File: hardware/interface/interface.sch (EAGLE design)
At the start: 3 parts

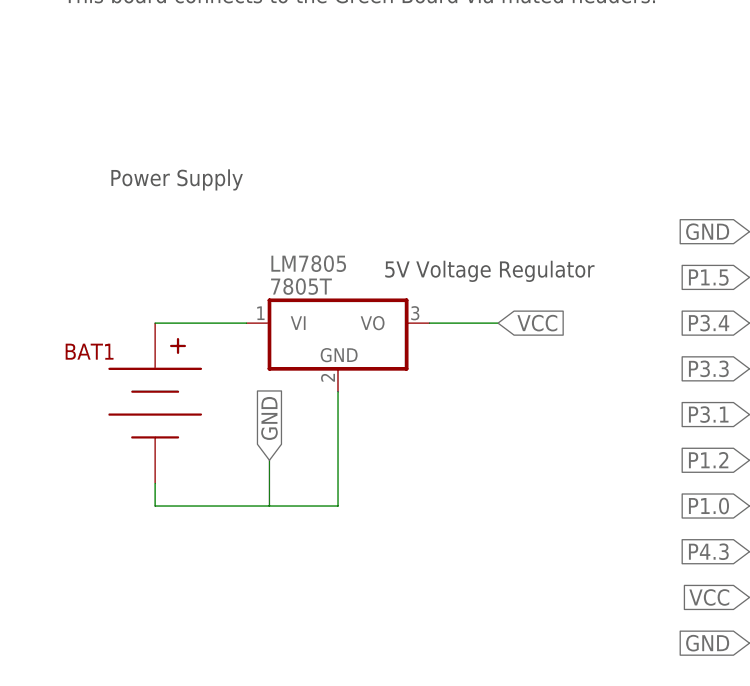
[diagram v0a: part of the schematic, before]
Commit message: add capacitors
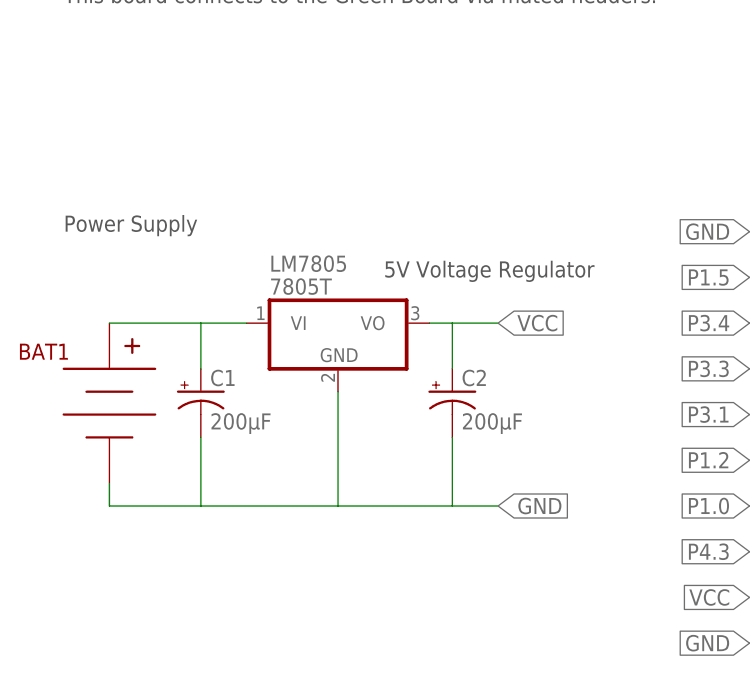
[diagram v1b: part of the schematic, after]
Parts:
- added C1, C2: 200µF, SparkFun-Capacitors:CAP_POLPTH1
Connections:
- net GND: now also C1.-, C2.-
- net N$1: now also C1.+
- net VCC: now also C2.+
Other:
- moved on the sheet: BAT1
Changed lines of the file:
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@@
 <part name="BAT1" library="SparkFun-Connectors" deviceset="BC9VPC" device=""/>
 <part name="LM7805" library="linear" deviceset="78*" device="T" technology="05"/>
+<part name="C1" library="SparkFun-Capacitors" deviceset="CAP_POL" device="PTH1" value="200µF"/>
+<part name="C2" library="SparkFun-Capacitors" deviceset="CAP_POL" device="PTH1" value="200µF"/>
 </parts>
 <sheets>
@@
 <text x="96.52" y="121.92" size="1.778" layer="97">LCD 128x64</text>
 <text x="25.4" y="109.22" size="1.778" layer="97">5V Voltage Regulator</text>
-<text x="-5.08" y="119.38" size="1.778" layer="97">Power Supply</text>
+<text x="-10.16" y="114.3" size="1.778" layer="97">Power Supply</text>
 <frame x1="-20.32" y1="35.56" x2="124.46" y2="154.94" columns="8" rows="5" layer="91"/>
 <text x="-10.16" y="144.78" size="1.778" layer="97">Connects LCD to Green Board and supplies power to the Green Board</text>
@@
 <instances>
 <instance part="U$1" gate="G$1" x="101.6" y="93.98"/>
-<instance part="BAT1" gate="G$1" x="0" y="96.52"/>
+<instance part="BAT1" gate="G$1" x="-5.08" y="96.52"/>
 <instance part="LM7805" gate="A1" x="20.32" y="104.14"/>
+<instance part="C1" gate="G$1" x="5.08" y="96.52"/>
+<instance part="C2" gate="G$1" x="33.02" y="96.52"/>
 </instances>
 <busses>
@@
 <wire x1="20.32" y1="96.52" x2="20.32" y2="83.82" width="0.1524" layer="91"/>
 <pinref part="BAT1" gate="G$1" pin="V-"/>
-<wire x1="20.32" y1="83.82" x2="12.7" y2="83.82" width="0.1524" layer="91"/>
-<wire x1="12.7" y1="83.82" x2="0" y2="83.82" width="0.1524" layer="91"/>
-<wire x1="0" y1="83.82" x2="0" y2="86.36" width="0.1524" layer="91"/>
-<wire x1="12.7" y1="83.82" x2="12.7" y2="88.9" width="0.1524" layer="91"/>
-<label x="12.7" y="88.9" size="1.778" layer="95" rot="R90" xref="yes"/>
+<wire x1="20.32" y1="83.82" x2="5.08" y2="83.82" width="0.1524" layer="91"/>
+<wire x1="5.08" y1="83.82" x2="-5.08" y2="83.82" width="0.1524" layer="91"/>
+<wire x1="-5.08" y1="83.82" x2="-5.08" y2="86.36" width="0.1524" layer="91"/>
+<wire x1="20.32" y1="83.82" x2="33.02" y2="83.82" width="0.1524" layer="91"/>
+<label x="38.1" y="83.82" size="1.778" layer="95" xref="yes"/>
+<pinref part="C1" gate="G$1" pin="-"/>
+<wire x1="33.02" y1="83.82" x2="38.1" y2="83.82" width="0.1524" layer="91"/>
+<wire x1="5.08" y1="91.44" x2="5.08" y2="83.82" width="0.1524" layer="91"/>
+<pinref part="C2" gate="G$1" pin="-"/>
+<wire x1="33.02" y1="91.44" x2="33.02" y2="83.82" width="0.1524" layer="91"/>
 </segment>
 </net>
@@
 <segment>
 <pinref part="LM7805" gate="A1" pin="VO"/>
-<wire x1="30.48" y1="104.14" x2="38.1" y2="104.14" width="0.1524" layer="91"/>
+<wire x1="30.48" y1="104.14" x2="33.02" y2="104.14" width="0.1524" layer="91"/>
 <label x="38.1" y="104.14" size="1.778" layer="95" xref="yes"/>
+<pinref part="C2" gate="G$1" pin="+"/>
+<wire x1="33.02" y1="104.14" x2="38.1" y2="104.14" width="0.1524" layer="91"/>
+<wire x1="33.02" y1="99.06" x2="33.02" y2="104.14" width="0.1524" layer="91"/>
 </segment>
 </net>
@@
 <pinref part="BAT1" gate="G$1" pin="V+"/>
 <pinref part="LM7805" gate="A1" pin="VI"/>
-<wire x1="0" y1="104.14" x2="10.16" y2="104.14" width="0.1524" layer="91"/>
+<wire x1="-5.08" y1="104.14" x2="5.08" y2="104.14" width="0.1524" layer="91"/>
+<pinref part="C1" gate="G$1" pin="+"/>
+<wire x1="5.08" y1="104.14" x2="10.16" y2="104.14" width="0.1524" layer="91"/>
+<wire x1="5.08" y1="99.06" x2="5.08" y2="104.14" width="0.1524" layer="91"/>
 </segment>
 </net>

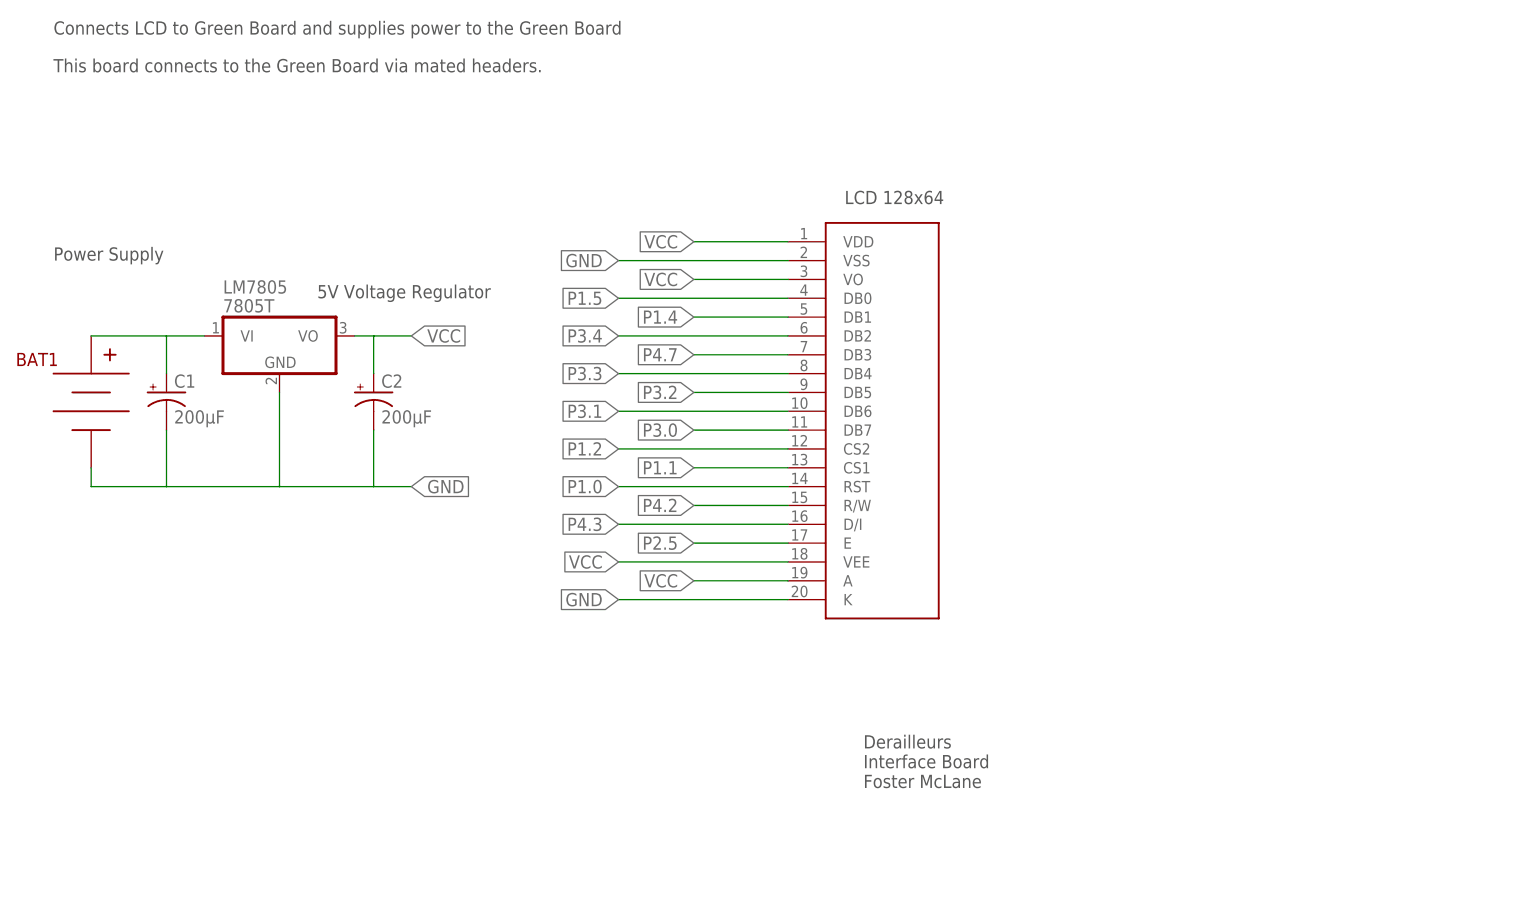
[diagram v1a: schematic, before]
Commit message: update interface schematic
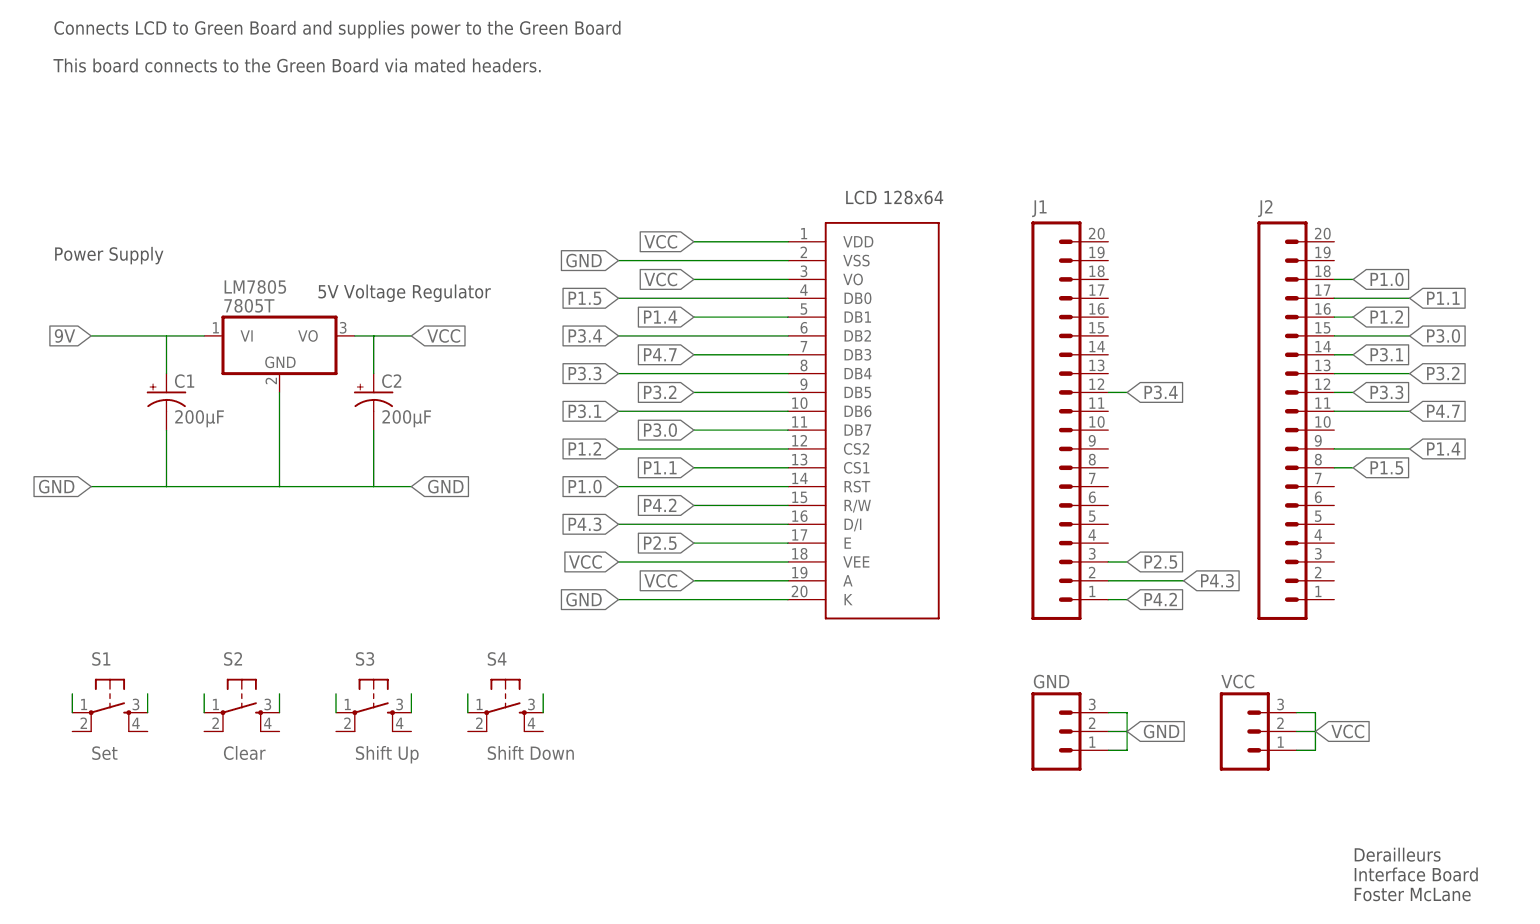
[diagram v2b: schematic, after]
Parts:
- removed BAT1: (no value), SparkFun-Connectors:BC9VPC
- added GND, VCC: (no value), SparkFun-Connectors:M03PTH
- added J1, J2: (no value), SparkFun-Connectors:M20
- added S1: Set, SparkFun-Retired:TAC_SWITCHPTH
- added S2: Clear, SparkFun-Retired:TAC_SWITCHPTH
- added S3: Shift Up, SparkFun-Retired:TAC_SWITCHPTH
- added S4: Shift Down, SparkFun-Retired:TAC_SWITCHPTH
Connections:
- removed net N$1: BAT1.V+, C1.+, LM7805.VI
- new net 9V: C1.+, LM7805.VI
- new net N$2: S1.1
- new net N$3: S1.3
- new net N$4: S2.1
- new net N$5: S2.3
- new net N$6: S3.1
- new net N$7: S3.3
- new net N$8: S4.1
- new net N$9: S4.3
- net GND: now also GND.1, GND.2, GND.3; no longer BAT1.V-
- net P1.0: now also J2.18
- net P1.1: now also J2.17
- net P1.2: now also J2.16
- net P1.4: now also J2.9
- net P1.5: now also J2.8
- net P2.5: now also J1.3
- net P3.0: now also J2.15
- net P3.1: now also J2.14
- net P3.2: now also J2.13
- net P3.3: now also J2.12
- net P3.4: now also J1.12
- net P4.2: now also J1.1
- net P4.3: now also J1.2
- net P4.7: now also J2.11
- net VCC: now also VCC.1, VCC.2, VCC.3

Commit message: finish boards
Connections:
- removed net N$2: S1.1
- removed net N$3: S1.3
- removed net N$4: S2.1
- removed net N$5: S2.3
- removed net N$6: S3.1
- removed net N$7: S3.3
- removed net N$8: S4.1
- removed net N$9: S4.3
- new net P2.0: J1.7, S1.3
- new net P2.6: J1.4, S2.3
- new net P3.5: J1.11, S3.3
- new net P3.6: J1.12, S4.3
- net GND: now also S1.1, S2.1, S3.1, S4.1
- net P3.4: now also J1.10; no longer J1.12
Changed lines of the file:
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@@
 </segment>
 <segment>
-<pinref part="J1" gate="G$1" pin="12"/>
-<wire x1="132.08" y1="96.52" x2="134.62" y2="96.52" width="0.1524" layer="91"/>
-<label x="134.62" y="96.52" size="1.778" layer="95" xref="yes"/>
+<pinref part="J1" gate="G$1" pin="10"/>
+<wire x1="132.08" y1="91.44" x2="134.62" y2="91.44" width="0.1524" layer="91"/>
+<label x="134.62" y="91.44" size="1.778" layer="95" xref="yes"/>
 </segment>
 </net>
@@
 <label x="134.62" y="50.8" size="1.778" layer="95" xref="yes"/>
 </segment>
+<segment>
+<pinref part="S1" gate="S" pin="1"/>
+<wire x1="-7.62" y1="53.34" x2="-7.62" y2="55.88" width="0.1524" layer="91"/>
+<label x="-7.62" y="55.88" size="1.778" layer="95" rot="R90" xref="yes"/>
+</segment>
+<segment>
+<pinref part="S2" gate="S" pin="1"/>
+<wire x1="10.16" y1="53.34" x2="10.16" y2="55.88" width="0.1524" layer="91"/>
+<label x="10.16" y="55.88" size="1.778" layer="95" rot="R90" xref="yes"/>
+</segment>
+<segment>
+<pinref part="S3" gate="S" pin="1"/>
+<wire x1="27.94" y1="53.34" x2="27.94" y2="55.88" width="0.1524" layer="91"/>
+<label x="27.94" y="55.88" size="1.778" layer="95" rot="R90" xref="yes"/>
+</segment>
+<segment>
+<pinref part="S4" gate="S" pin="1"/>
+<wire x1="45.72" y1="53.34" x2="45.72" y2="55.88" width="0.1524" layer="91"/>
+<label x="45.72" y="55.88" size="1.778" layer="95" rot="R90" xref="yes"/>
+</segment>
 </net>
 <net name="VCC" class="0">
@@
 </segment>
 </net>
-<net name="N$2" class="0">
-<segment>
-<pinref part="S1" gate="S" pin="1"/>
-<wire x1="-7.62" y1="53.34" x2="-7.62" y2="55.88" width="0.1524" layer="91"/>
-</segment>
-</net>
-<net name="N$3" class="0">
+<net name="P2.0" class="0">
 <segment>
 <pinref part="S1" gate="S" pin="3"/>
 <wire x1="2.54" y1="53.34" x2="2.54" y2="55.88" width="0.1524" layer="91"/>
+<label x="2.54" y="55.88" size="1.778" layer="95" rot="R90" xref="yes"/>
+</segment>
+<segment>
+<pinref part="J1" gate="G$1" pin="7"/>
+<wire x1="132.08" y1="83.82" x2="134.62" y2="83.82" width="0.1524" layer="91"/>
+<label x="134.62" y="83.82" size="1.778" layer="95" xref="yes"/>
 </segment>
 </net>
-<net name="N$4" class="0">
-<segment>
-<pinref part="S2" gate="S" pin="1"/>
-<wire x1="10.16" y1="53.34" x2="10.16" y2="55.88" width="0.1524" layer="91"/>
-</segment>
-</net>
-<net name="N$5" class="0">
+<net name="P2.6" class="0">
 <segment>
 <pinref part="S2" gate="S" pin="3"/>
 <wire x1="20.32" y1="53.34" x2="20.32" y2="55.88" width="0.1524" layer="91"/>
+<label x="20.32" y="55.88" size="1.778" layer="95" rot="R90" xref="yes"/>
+</segment>
+<segment>
+<pinref part="J1" gate="G$1" pin="4"/>
+<wire x1="132.08" y1="76.2" x2="142.24" y2="76.2" width="0.1524" layer="91"/>
+<label x="142.24" y="76.2" size="1.778" layer="95" xref="yes"/>
 </segment>
 </net>
-<net name="N$6" class="0">
-<segment>
-<pinref part="S3" gate="S" pin="1"/>
-<wire x1="27.94" y1="53.34" x2="27.94" y2="55.88" width="0.1524" layer="91"/>
-</segment>
-</net>
-<net name="N$7" class="0">
+<net name="P3.5" class="0">
 <segment>
 <pinref part="S3" gate="S" pin="3"/>
 <wire x1="38.1" y1="53.34" x2="38.1" y2="55.88" width="0.1524" layer="91"/>
+<label x="38.1" y="55.88" size="1.778" layer="95" rot="R90" xref="yes"/>
+</segment>
+<segment>
+<pinref part="J1" gate="G$1" pin="11"/>
+<wire x1="132.08" y1="93.98" x2="142.24" y2="93.98" width="0.1524" layer="91"/>
+<label x="142.24" y="93.98" size="1.778" layer="95" xref="yes"/>
 </segment>
 </net>
-<net name="N$8" class="0">
-<segment>
-<pinref part="S4" gate="S" pin="1"/>
-<wire x1="45.72" y1="53.34" x2="45.72" y2="55.88" width="0.1524" layer="91"/>
-</segment>
-</net>
-<net name="N$9" class="0">
+<net name="P3.6" class="0">
 <segment>
 <pinref part="S4" gate="S" pin="3"/>
 <wire x1="55.88" y1="53.34" x2="55.88" y2="55.88" width="0.1524" layer="91"/>
+<label x="55.88" y="55.88" size="1.778" layer="95" rot="R90" xref="yes"/>
+</segment>
+<segment>
+<pinref part="J1" gate="G$1" pin="12"/>
+<wire x1="132.08" y1="96.52" x2="134.62" y2="96.52" width="0.1524" layer="91"/>
+<label x="134.62" y="96.52" size="1.778" layer="95" xref="yes"/>
 </segment>
 </net>
